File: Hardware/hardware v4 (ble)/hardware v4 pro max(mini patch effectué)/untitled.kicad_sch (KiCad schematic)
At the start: 24 parts, among them J1 SM06B-SRSS-TB, Q1 2N7002K, SW1 Int, U2 LTC4065AEDC, U3 LDLN022PU33R

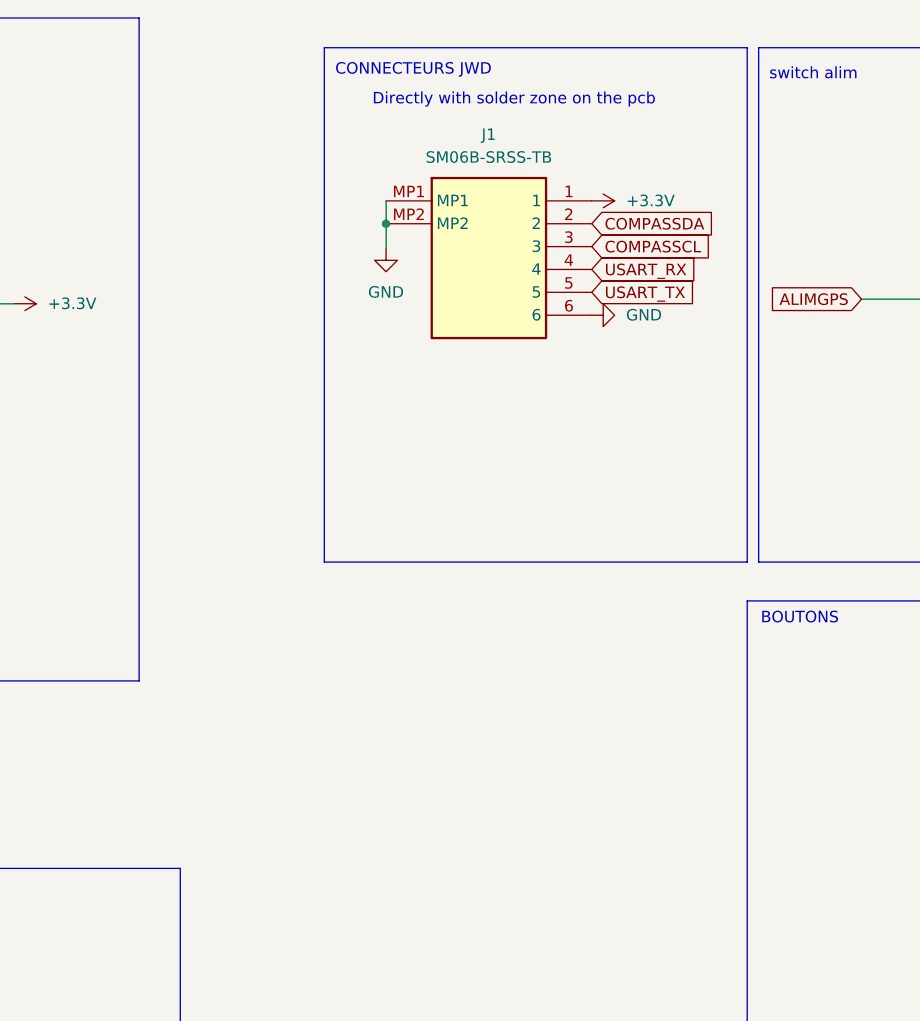
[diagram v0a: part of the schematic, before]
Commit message: board v5 gps 25Hz !!
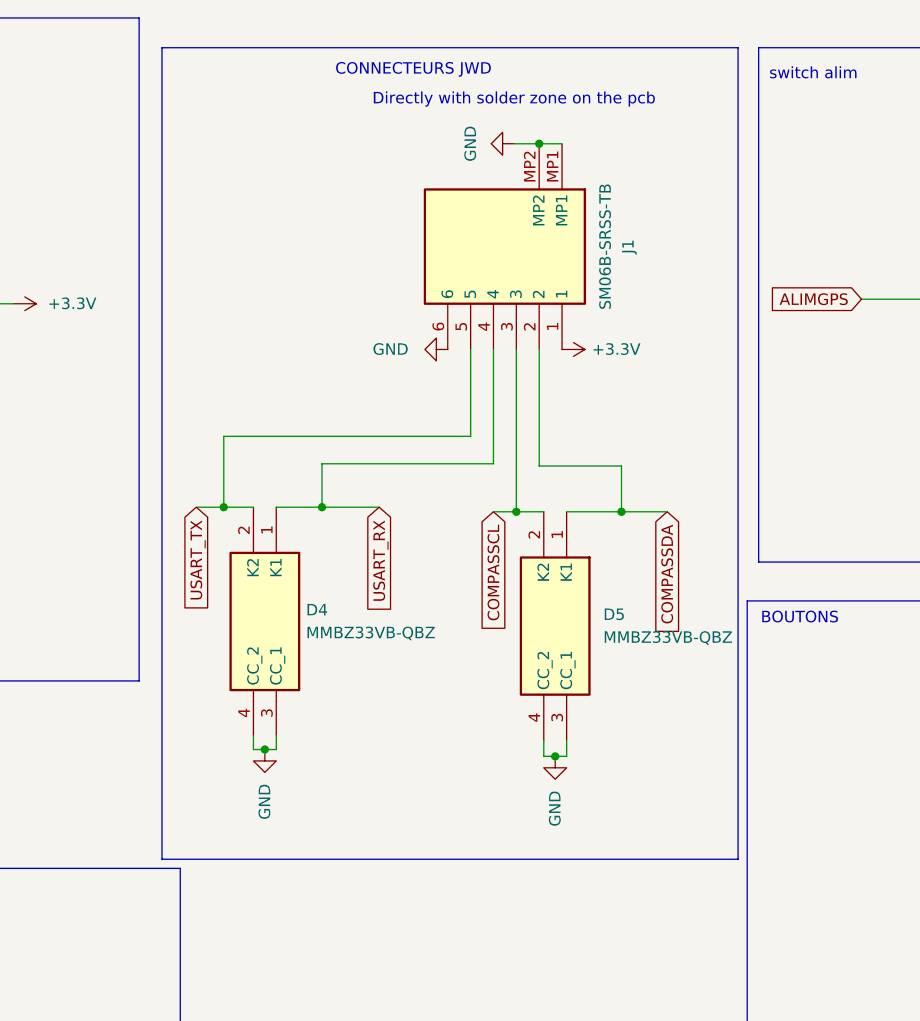
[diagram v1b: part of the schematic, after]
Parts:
- added D4, D5: MMBZ33VB-QBZ, MMBZ33VB-QBZ:BC847BQBZ, symbol MMBZ33VB-QBZ:MMBZ33VB-QBZ
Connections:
- net COMPASSCL: now also D5.2 (K2)
- net COMPASSDA: now also D5.1 (K1)
- net GND: now also D4.3 (CC_1), D4.4 (CC_2), D5.3 (CC_1), D5.4 (CC_2)
- net USART_RX: now also D4.1 (K1)
- net USART_TX: now also D4.2 (K2)
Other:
- moved on the sheet: J1

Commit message: yhry
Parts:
- J1: footprint SM06B-SRSS:SM06BSRSSTB -> Connector_JST:JST_SH_SM06B-SRSS-TB_1x06-1MP_P1.00mm_Horizontal
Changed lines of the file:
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@@
 			)
 		)
-		(property "Footprint" "SM06B-SRSS:SM06BSRSSTB"
+		(property "Footprint" "Connector_JST:JST_SH_SM06B-SRSS-TB_1x06-1MP_P1.00mm_Horizontal"
 			(at 92.278 46.736 0)
 			(effects
